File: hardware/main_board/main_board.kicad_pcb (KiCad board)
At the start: 4 copper layers, 26.6 x 106.5 mm, 33 parts, among them J1 eConn_02x03_Odd_Even, P1 CONN_01X02, Q1 DMG3415U, SW1 SW_DPDT_x2, U1 MCP73831/2, U2 AP2112, U3 Si1145, U4 MCP9808, U5 ESP-WROOM-32D, U6 MMA8451Q

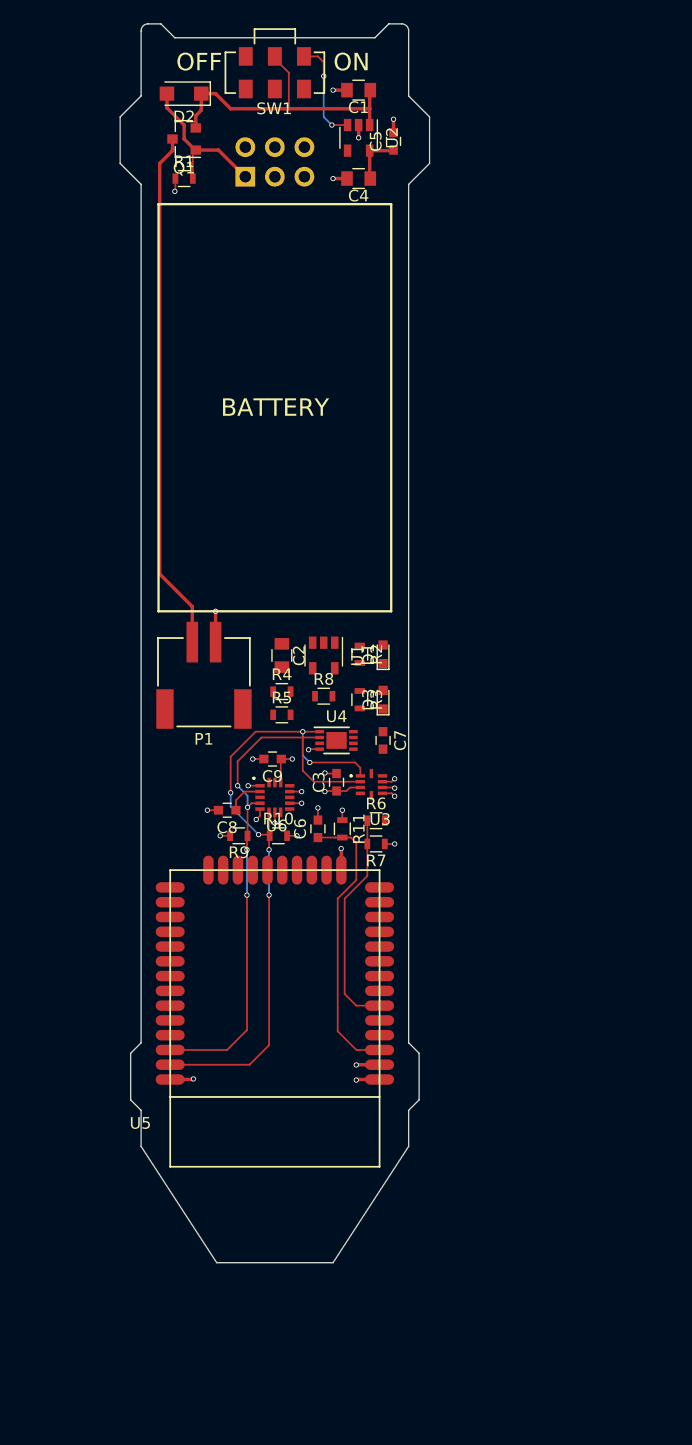
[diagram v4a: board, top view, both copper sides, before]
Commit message: Finished routing board
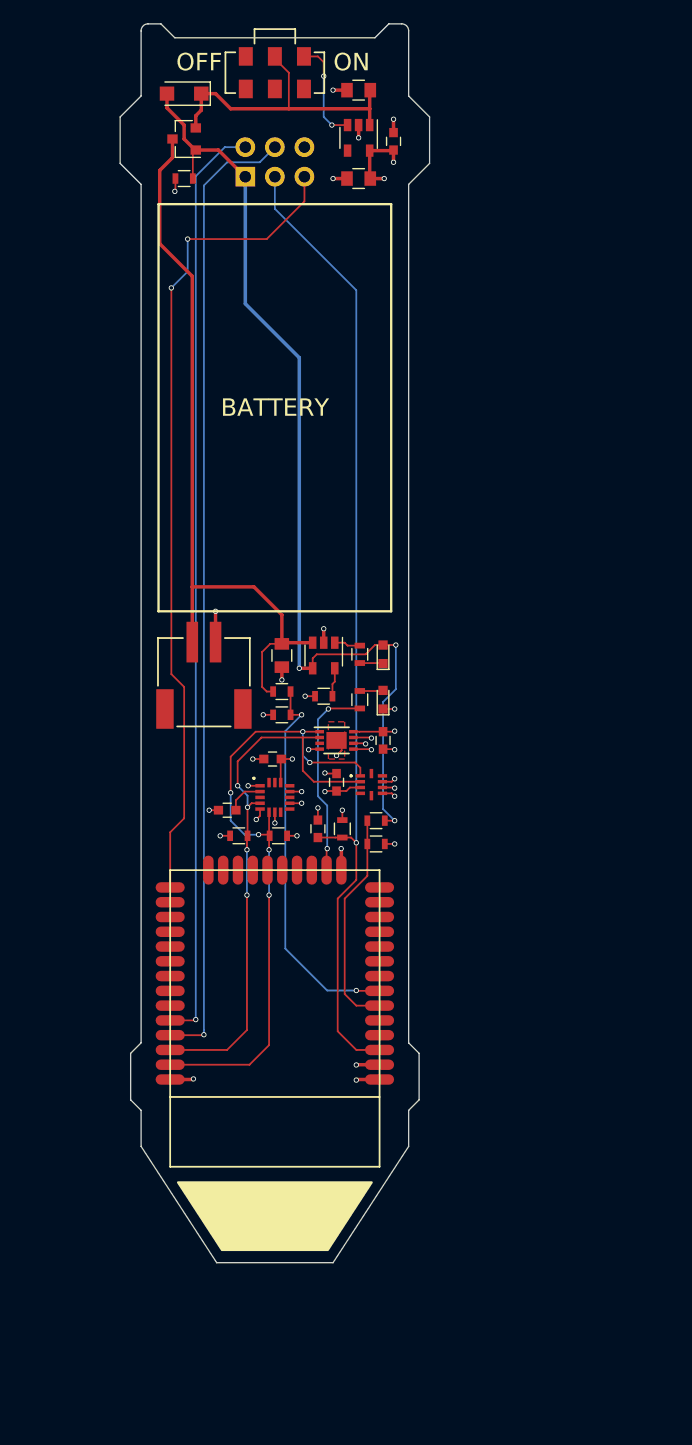
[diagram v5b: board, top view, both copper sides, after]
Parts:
- turned R5 to 180 degrees
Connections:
- U4 pad 9: Net-(U4-Pad9) -> GND
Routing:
- net /PROG_RXD: track 0.00 -> 83.4 mm, vias 0 -> 1
- net /PROG_TXD: track 0.00 -> 80.0 mm, vias 0 -> 1
- net /GPIO0: track 0.00 -> 70.8 mm, vias 0 -> 2
- net +5V: track 13.7 -> 84.3 mm, vias 0 -> 3
- net /RESET: track 24.6 -> 84.8 mm, vias 0 -> 1
- net /BAT_SENSE: track 0.00 -> 33.2 mm, vias 0 -> 2
- net +BATT: track 44.9 -> 64.9 mm
- net /LED: track 0.00 -> 17.3 mm, vias 0 -> 2
- net GND: track 24.3 -> 35.5 mm, vias 19 -> 29
- net +3V3: track 19.4 -> 25.2 mm, vias 10 -> 13
- net Net-(R8-Pad2): track 0.00 -> 2.48 mm
- net Net-(R2-Pad1): track 0.00 -> 2.25 mm
- net Net-(D3-Pad2): track 0.00 -> 2.02 mm
- net Net-(D1-Pad1): track 0.00 -> 2.02 mm
- net /SDA: track 54.6 -> 55.3 mm
- added copper zone on F.Cu, net GND
